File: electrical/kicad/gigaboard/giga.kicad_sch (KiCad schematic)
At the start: 61 parts, among them J1 Conn_01x04, J10 Conn_01x04, J11 Conn_01x06, J2 Conn_02x03_Top_Bottom, J3 Conn_01x04, J4 Conn_02x03_Top_Bottom, J5 Conn_02x03_Top_Bottom, J6 Conn_01x04, J7 Conn_02x03_Top_Bottom, J8 Conn_01x04, J9 Conn_02x03_Top_Bottom, U1 AHT20, U2 AS5600, U3 AS5600, U4 AS5600, U5 AS5600, U6 AS5600

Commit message: add(kicad): pbd files
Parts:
- removed A1: Arduino_Giga_R1_WiFi_Shield, PCM_arduino-library:Arduino_Giga_R1_WiFi_Shield, symbol PCM_arduino-library:Arduino_Giga_R1_WiFi_Shield_1
- removed C1, C2, C3, C4, C5, C6, C7, C8, C9: 100uF, Capacitor_THT:C_Radial_D4.0mm_H5.0mm_P1.50mm, symbol ControlPCB-rescue:CP1_Small
- removed D1, D2, D3, D4, D5: ~, TMC2209_SILENTSTEPSTICK:MODULE_TMC2209_SILENTSTEPSTICK, symbol Motor_Driver:TMC2209
- removed D6: MD10C_DC_Driver, symbol Motor_Driver:MD10C_DC_Driver
- removed J1, J10, J3, J6, J8: Conn_01x04, symbol Connector_Generic:Conn_01x04
- removed J11: Conn_01x06, symbol Connector_Generic:Conn_01x06
- removed J2, J4, J5, J7, J9: Conn_02x03_Top_Bottom, symbol Connector_Generic:Conn_02x03_Top_Bottom
- removed R1, R13, R2, R6, R9: 10k, symbol Device:R
- removed R10, R14, R16, R17, R3, R5, R7: 100k, symbol Device:R
- removed R11, R12, R15, R4, R8: 1K, symbol Device:R
- removed R18, R19, R20, R21, R22, R23, R24, R25, R26, R27: 3.9K, symbol Device:R
- removed S1: BMX160_9axis, symbol Sensors:BMX160_9axis
- removed U1: AHT20, AHT20:PSON100P300X300X110-6N, symbol AHT20:AHT20
- removed U2, U3, U4, U5, U6: AS5600, AS5600:AS5600, symbol AS5600:AS5600
- added A?: Arduino_Giga_R1_WiFi_Shield, PCM_arduino-library:Arduino_Giga_R1_WiFi_Shield, symbol PCM_arduino-library:Arduino_Giga_R1_WiFi_Shield_1
- added C? (x9): 100uF, Capacitor_THT:C_Radial_D4.0mm_H5.0mm_P1.50mm, symbol ControlPCB-rescue:CP1_Small
- added D? (x5): ~, TMC2209_SILENTSTEPSTICK:MODULE_TMC2209_SILENTSTEPSTICK, symbol Motor_Driver:TMC2209
- added D?: MD10C_DC_Driver, symbol Motor_Driver:MD10C_DC_Driver
- added J? (x5): Conn_01x04, symbol Connector_Generic:Conn_01x04
- added J? (x5): Conn_02x03_Top_Bottom, symbol Connector_Generic:Conn_02x03_Top_Bottom
- added J?: Conn_01x06, symbol Connector_Generic:Conn_01x06
- added R? (x5): 10k, symbol Device:R
- added R? (x5): 1K, symbol Device:R
- added R? (x7): 100k, symbol Device:R
- added R? (x10): 3.9K, symbol Device:R
- added S?: BMX160_9axis, symbol Sensors:BMX160_9axis
- added U? (x5): AS5600, AS5600:AS5600, symbol AS5600:AS5600
- added U?: AHT20, AHT20:PSON100P300X300X110-6N, symbol AHT20:AHT20
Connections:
- net +12V: now also C?.1, C?.1, C?.1, C?.1, C?.1, D?.8 (VM), D?.8 (VM), D?.8 (VM), D?.8 (VM), D?.8 (VM)
- net +3.3V: now also C?.1, J?.2 (Pin_2), U?.2 (VDD3V3), U?.2 (VDD3V3), U?.2 (VDD3V3), U?.2 (VDD3V3), U?.2 (VDD3V3)
- net +5V: now also A?.5V1 (5V), A?.5V2 (SPI_5V), A?.5V3 (5V), A?.5V4 (5V), A?.5V5 (5V), C?.1, D?.2 (VIO), D?.2 (VIO), D?.2 (VIO), D?.2 (VIO), D?.2 (VIO), J?.1 (Pin_1), J?.1 (Pin_1), J?.1 (Pin_1), J?.1 (Pin_1), J?.1 (Pin_1), J?.1 (Pin_1), J?.2 (Pin_2), J?.2 (Pin_2), J?.2 (Pin_2), J?.2 (Pin_2), J?.2 (Pin_2), J?.3 (Pin_3), J?.3 (Pin_3), J?.3 (Pin_3), J?.3 (Pin_3), J?.3 (Pin_3), R?.1, R?.1, R?.1, R?.1, R?.1, R?.1, R?.1, R?.1, R?.1, R?.1, R?.1, R?.1, R?.1, R?.1, R?.1, U?.1 (VDD5V), U?.1 (VDD5V), U?.1 (VDD5V), U?.1 (VDD5V), U?.1 (VDD5V)
- net D22: now also D?.18 (DIAG)
- net D23: now also D?.17 (INDEX)
- net D24: now also D?.18 (DIAG)
- net D25: now also D?.17 (INDEX)
- net D26: now also D?.18 (DIAG)
- net D27: now also D?.17 (INDEX)
- net D28: now also D?.18 (DIAG)
- net D29: now also D?.17 (INDEX)
- net D30: now also D?.18 (DIAG)
- net D31: now also D?.17 (INDEX)
- net DIR1: now also A?.D54, D?.9 (DIR), D?.9 (DIR), D?.9 (DIR), D?.9 (DIR), D?.9 (DIR)
- net DIR2: now also A?.D57
- net DIR3: now also A?.D60
- net DIR4: now also A?.D63
- net DIR5: now also A?.D66
- net ENA1: now also A?.D56, D?.16 (~{EN}), D?.16 (~{EN}), D?.16 (~{EN}), D?.16 (~{EN}), D?.16 (~{EN}), R?.2, R?.2, R?.2, R?.2, R?.2
- net ENA2: now also A?.D59
- net ENA3: now also A?.D62
- net ENA4: now also A?.D65
- net ENA5: now also A?.D68
- net GND: now also A?.GND1 (GND), A?.GND10 (GND), A?.GND11 (GND), A?.GND12 (GND), A?.GND13 (GND), A?.GND14 (GND), A?.GND15 (GND), A?.GND2 (GND), A?.GND3 (GND), A?.GND4 (SPI_GND), A?.GND5 (GND), A?.GND6 (GND), A?.GND7 (GND), A?.GND8 (GND), A?.GND9 (GND), C?.2, C?.2, C?.2, C?.2, C?.2, C?.2, C?.2, C?.2, C?.2, D?.1 (GND), D?.1 (GND), D?.1 (GND), D?.1 (GND), D?.1 (GND), D?.2 (GND), D?.7 (GND), D?.7 (GND), D?.7 (GND), D?.7 (GND), D?.7 (GND), J?.3 (Pin_3), R?.2, R?.2, R?.2, R?.2, R?.2, S?.2 (GND), U?.4 (GND), U?.4 (GND), U?.4 (GND), U?.4 (GND), U?.4 (GND), U?.5 (GND), U?.8 (DIR), U?.8 (DIR), U?.8 (DIR), U?.8 (DIR), U?.8 (DIR)
- net OUT: now also J?.6 (Pin_6), U?.3 (OUT), U?.3 (OUT), U?.3 (OUT), U?.3 (OUT), U?.3 (OUT)
- net PUL1: now also A?.D55, D?.10 (STEP), D?.10 (STEP), D?.10 (STEP), D?.10 (STEP), D?.10 (STEP)
- net PUL2: now also A?.D58
- net PUL3: now also A?.D61
- net PUL4: now also A?.D64
- net PUL5: now also A?.D67
- net SCL1: now also J?.4 (Pin_4), R?.2, R?.2, R?.2, R?.2, R?.2, U?.7 (SCL), U?.7 (SCL), U?.7 (SCL), U?.7 (SCL), U?.7 (SCL)
- net SCL2: now also R?.1, S?.3 (SCL), U?.3 (SCL)
- net SDA1: now also J?.5 (Pin_5), R?.2, R?.2, R?.2, R?.2, R?.2, U?.6 (SDA), U?.6 (SDA), U?.6 (SDA), U?.6 (SDA), U?.6 (SDA)
- net SDA2: now also R?.1, S?.4 (SDA), U?.4 (SDA)
- net URT1: now also A?.D0 (D0/RX0), A?.D1 (D1/TX0), D?.12 (UART), D?.12 (UART), D?.12 (UART), D?.12 (UART), D?.12 (UART), R?.2, R?.2, R?.2, R?.2, R?.2
- net URT2: now also A?.D18 (D18/TX1), A?.D19 (D19/RX1)
- net URT3: now also A?.D16 (D16/TX2), A?.D17 (D17/RX2)
- net URT4: now also A?.D14 (D14/TX3), A?.D15 (D15/RX3)
- net URT5: now also A?.D20 (D20/SDA), A?.D21 (D21/SCL)
- net cs: now also S?.7 (CSB)
- new net: D?.6 (2B), J?.1 (Pin_1) (x5)
- new net: D?.5 (2A), J?.2 (Pin_2) (x5)
- new net: D?.4 (1A), J?.3 (Pin_3) (x5)
- new net: D?.3 (1B), J?.4 (Pin_4) (x5)
- new net: D?.11 (PDN), R?.1 (x5)
- new net: D?.15 (MS1), J?.4 (Pin_4), R?.1 (x5)
- new net: D?.14 (MS2), J?.5 (Pin_5) (x5)
- new net: D?.13 (SPRD), J?.6 (Pin_6) (x5)
- new net: C?.1, S?.1 (VCC)
- new net: C?.1, R?.2, R?.2, U?.2 (VDD)
- new net: U?.1 (NC), U?.6 (NC)

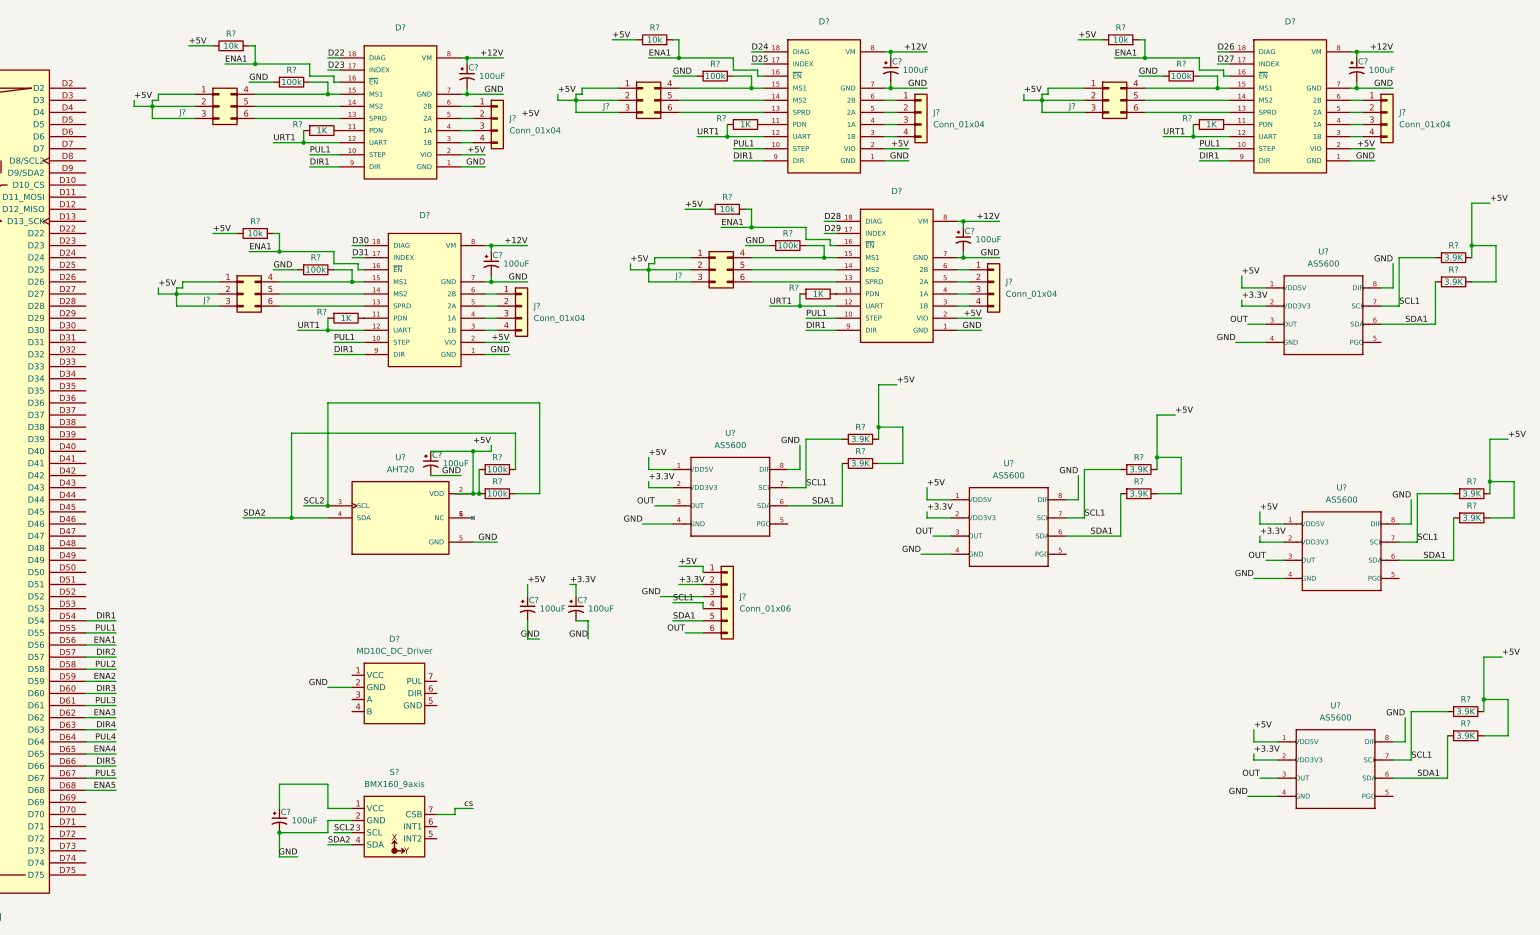
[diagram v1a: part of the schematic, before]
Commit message: update(giga): change symbols
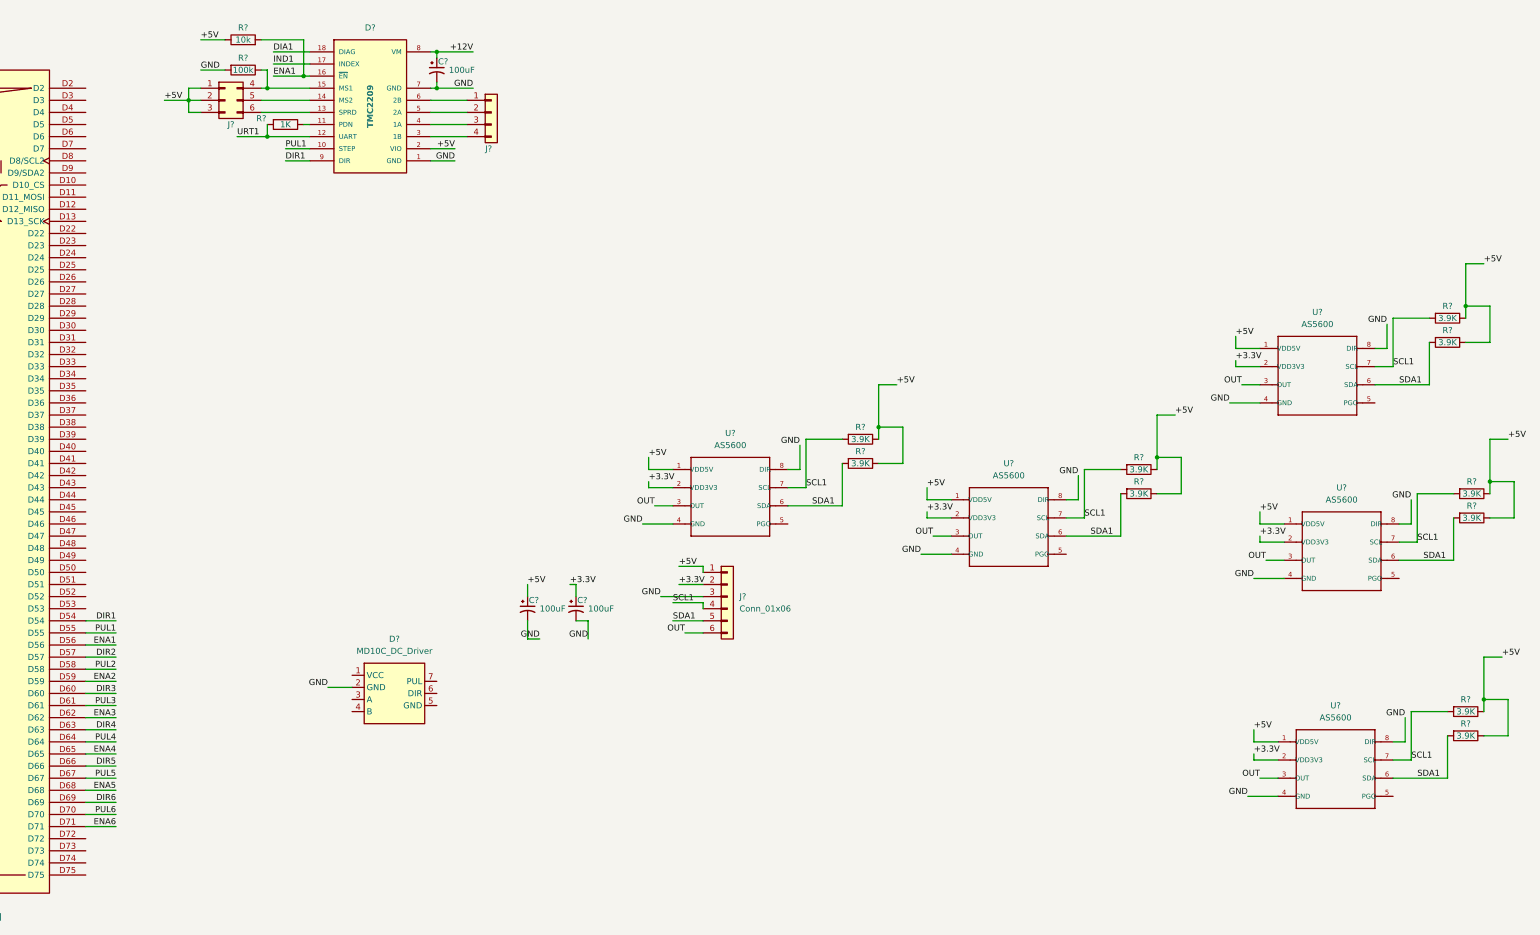
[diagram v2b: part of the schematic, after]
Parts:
- removed C? (x6): 100uF, Capacitor_THT:C_Radial_D4.0mm_H5.0mm_P1.50mm, symbol ControlPCB-rescue:CP1_Small
- removed D? (x5): ~, TMC2209_SILENTSTEPSTICK:MODULE_TMC2209_SILENTSTEPSTICK, symbol Motor_Driver:TMC2209
- removed J? (x4): Conn_01x04, symbol Connector_Generic:Conn_01x04
- removed J? (x4): Conn_02x03_Top_Bottom, symbol Connector_Generic:Conn_02x03_Top_Bottom
- removed R? (x4): 10k, symbol Device:R
- removed R? (x4): 1K, symbol Device:R
- removed R? (x6): 100k, symbol Device:R
- removed S?: BMX160_9axis, symbol Sensors:BMX160_9axis
- removed U?: AHT20, AHT20:PSON100P300X300X110-6N, symbol AHT20:AHT20
- added D?: TMC2209, TMC2209_SILENTSTEPSTICK:MODULE_TMC2209_SILENTSTEPSTICK, symbol Motor_Driver:TMC2209
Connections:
- net +12V: now also D?.8 (VM)
- net +5V: now also D?.2 (VIO)
- net DIR1: now also D?.9 (DIR)
- net ENA1: now also D?.16 (~{EN})
- net GND: now also D?.1 (GND), D?.7 (GND)
- net PUL1: now also D?.10 (STEP)
- net URT1: now also D?.12 (UART)
- net DIR6: now reaches A?.D69
- net PUL6: now reaches A?.D70
- net ENA6: now reaches A?.D71
- net at J?.4 (Pin_4), R?.1: now also D?.15 (MS1)
- net at J?.1 (Pin_1): now also D?.6 (2B)
- net at J?.2 (Pin_2): now also D?.5 (2A)
- net at J?.3 (Pin_3): now also D?.4 (1A)
- net at J?.4 (Pin_4): now also D?.3 (1B)
- net at J?.5 (Pin_5): now also D?.14 (MS2)
- net at J?.6 (Pin_6): now also D?.13 (SPRD)
- net at R?.1: now also D?.11 (PDN)
- new net DIA1: D?.18 (DIAG)
- new net IND1: D?.17 (INDEX)
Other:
- moved on the sheet: C?, J?, R?, U?

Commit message: update(giga): sym structure, comms module
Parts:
- removed C? (x3): 100uF, Capacitor_THT:C_Radial_D4.0mm_H5.0mm_P1.50mm, symbol ControlPCB-rescue:CP1_Small
- removed D?: MD10C_DC_Driver, symbol Motor_Driver:MD10C_DC_Driver
- removed D?: TMC2209, TMC2209_SILENTSTEPSTICK:MODULE_TMC2209_SILENTSTEPSTICK, symbol Motor_Driver:TMC2209
- removed J?: Conn_01x06, symbol Connector_Generic:Conn_01x06
- removed J?: Conn_01x04, symbol Connector_Generic:Conn_01x04
- removed J?: Conn_02x03_Top_Bottom, symbol Connector_Generic:Conn_02x03_Top_Bottom
- removed R?: 100k, symbol Device:R
- removed R? (x10): 3.9K, symbol Device:R
- removed R?: 10k, symbol Device:R
- removed R?: 1K, symbol Device:R
- removed U? (x5): AS5600, AS5600:AS5600, symbol AS5600:AS5600
- added C? (x6): 100uF, Capacitor_THT:C_Radial_D4.0mm_H5.0mm_P1.50mm, symbol ControlPCB-rescue:CP1_Small
- added D? (x6): TMC2209, TMC2209_SILENTSTEPSTICK:MODULE_TMC2209_SILENTSTEPSTICK, symbol Motor_Driver:TMC2209
- added E? (x6): AS5600, symbol Sensors:AS5600_Encoder
- added J? (x13): Conn_01x04, symbol Connector_Generic:Conn_01x04
- added J? (x2): Conn_01x02, symbol Connector_Generic:Conn_01x02
- added J? (x6): Conn_02x04_Counter_Clockwise, symbol Connector_Generic:Conn_02x04_Counter_Clockwise
- added J?: Screw_Terminal_01x03, symbol Connector:Screw_Terminal_01x03
- added R? (x6): 10k, symbol Device:R
- added R? (x6): 100k, symbol Device:R
- added S?: INA219, symbol Sensors:INA219_Current_Voltage_Sensor
- added U?: TCA9548A, 2717:MODULE_2717, symbol Comms:TCA9548A
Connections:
- net +3.3V: now also A?.3V1 (3.3V)
- net +5V: now also D?.2 (VIO), D?.2 (VIO), D?.2 (VIO), D?.2 (VIO), D?.2 (VIO), D?.2 (VIO), E?.1 (VCC), E?.1 (VCC), E?.1 (VCC), E?.1 (VCC), E?.1 (VCC), E?.1 (VCC), J?.1 (Pin_1), J?.1 (Pin_1), J?.1 (Pin_1), J?.1 (Pin_1), J?.1 (Pin_1), J?.1 (Pin_1), J?.2 (Pin_2), J?.2 (Pin_2), J?.2 (Pin_2), J?.2 (Pin_2), J?.2 (Pin_2), J?.2 (Pin_2), J?.3 (Pin_3), J?.3 (Pin_3), J?.3 (Pin_3), J?.3 (Pin_3), J?.3 (Pin_3), J?.3 (Pin_3), J?.3 (Pin_3), R?.1, R?.1, R?.1, R?.1, R?.1, R?.1, S?.4 (VCC)
- net GND: now also C?.2, C?.2, C?.2, C?.2, C?.2, C?.2, D?.1 (GND), D?.1 (GND), D?.1 (GND), D?.1 (GND), D?.1 (GND), D?.1 (GND), D?.7 (GND), D?.7 (GND), D?.7 (GND), D?.7 (GND), D?.7 (GND), D?.7 (GND), E?.3 (GND), E?.3 (GND), E?.3 (GND), E?.3 (GND), E?.3 (GND), E?.3 (GND), E?.7 (GPO), E?.7 (GPO), E?.7 (GPO), E?.7 (GPO), E?.7 (GPO), E?.7 (GPO), J?.2 (Pin_2), R?.2, R?.2, R?.2, R?.2, R?.2, R?.2, S?.2 (VIN-), S?.3 (GND)
- net DIR1: no longer names the net of A?.D54
- net DIR2: no longer names the net of A?.D57
- net DIR3: no longer names the net of A?.D60
- net DIR4: no longer names the net of A?.D63
- net DIR5: no longer names the net of A?.D66
- net DIR6: no longer names the net of A?.D69
- net ENA1: no longer names the net of A?.D56
- net ENA2: no longer names the net of A?.D59
- net ENA3: no longer names the net of A?.D62
- net ENA4: no longer names the net of A?.D65
- net ENA5: no longer names the net of A?.D68
- net ENA6: no longer names the net of A?.D71
- net PUL1: no longer names the net of A?.D55
- net PUL2: no longer names the net of A?.D58
- net PUL3: no longer names the net of A?.D61
- net PUL4: no longer names the net of A?.D64
- net PUL5: no longer names the net of A?.D67
- net PUL6: no longer names the net of A?.D70
- net URT1: no longer names the net of A?.D0 (D0/RX0)
- net URT1: no longer A?.D1 (D1/TX0)
- net URT2: no longer names the net of A?.D18 (D18/TX1)
- net URT2: no longer A?.D19 (D19/RX1)
- net URT3: no longer names the net of A?.D16 (D16/TX2)
- net URT3: no longer A?.D17 (D17/RX2)
- net URT4: no longer names the net of A?.D14 (D14/TX3)
- net URT4: no longer A?.D15 (D15/RX3)
- net URT5: no longer names the net of A?.D20 (D20/SDA)
- net URT5: no longer A?.D21 (D21/SCL)
- new net: D?.11 (PDN), D?.12 (UART), J?.5 (Pin_5) (x6)
- new net: D?.13 (SPRD), J?.6 (Pin_6) (x6)
- new net: D?.14 (MS2), J?.7 (Pin_7) (x6)
- new net: D?.15 (MS1), J?.8 (Pin_8), R?.1 (x6)
- new net: D?.3 (1B), J?.4 (Pin_4) (x6)
- new net: D?.4 (1A), J?.3 (Pin_3) (x6)
- new net: D?.5 (2A), J?.2 (Pin_2) (x6)
- new net: D?.6 (2B), J?.1 (Pin_1) (x6)
- new net +4S: J?.1 (Pin_1), S?.1 (VIN+)
- new net AS1_DIR: E?.4 (DIR)
- new net AS1_OUT: E?.2 (OUT)
- new net AS1_SCL: E?.6 (SDA)
- new net AS1_SDA: E?.5 (SCL)
- new net AS2_DIR: E?.4 (DIR)
- new net AS2_OUT: E?.2 (OUT)
- new net AS2_SCL: E?.6 (SDA)
- new net AS2_SDA: E?.5 (SCL)
- new net AS3_DIR: E?.4 (DIR)
- new net AS3_OUT: E?.2 (OUT)
- new net AS3_SCL: E?.6 (SDA)
- new net AS3_SDA: E?.5 (SCL)
- new net AS4_DIR: E?.4 (DIR)
- new net AS4_OUT: E?.2 (OUT)
- new net AS4_SCL: E?.6 (SDA)
- new net AS4_SDA: E?.5 (SCL)
- new net AS5_DIR: E?.4 (DIR)
- new net AS5_OUT: E?.2 (OUT)
- new net AS5_SCL: E?.6 (SDA)
- new net AS5_SDA: E?.5 (SCL)
- new net AS6_DIR: E?.4 (DIR)
- new net AS6_OUT: E?.2 (OUT)
- new net AS6_SCL: E?.6 (SDA)
- new net AS6_SDA: E?.5 (SCL)
- new net DC1_CHA: J?.3 (Pin_3)
- new net DC1_CHB: J?.4 (Pin_4)
- new net DC1_DIR: J?.2 (Pin_2)
- new net DC1_PWM: J?.1 (Pin_1)
- new net DC2_CHA: J?.3 (Pin_3)
- new net DC2_CHB: J?.4 (Pin_4)
- new net DC2_DIR: J?.2 (Pin_2)
- new net DC2_PWM: J?.1 (Pin_1)
- new net DC3_CHA: J?.3 (Pin_3)
- new net DC3_CHB: J?.4 (Pin_4)
- new net DC3_DIR: J?.2 (Pin_2)
- new net DC3_PWM: J?.1 (Pin_1)
- new net DC4_CHA: J?.3 (Pin_3)
- new net DC4_CHB: J?.4 (Pin_4)
- new net DC4_DIR: J?.2 (Pin_2)
- new net DC4_PWM: J?.1 (Pin_1)
- new net DC5_CHA: J?.3 (Pin_3)
- new net DC5_CHB: J?.4 (Pin_4)
- new net DC5_DIR: J?.2 (Pin_2)
- new net DC5_PWM: J?.1 (Pin_1)
- new net DC6_CHA: J?.3 (Pin_3)
- new net DC6_CHB: J?.4 (Pin_4)
- new net DC6_DIR: J?.2 (Pin_2)
- new net DC6_PWM: J?.1 (Pin_1)
- new net INA_SCL: S?.6 (SDA)
- new net INA_SDA: S?.5 (SCL)
- new net NAN0_TX: J?.2 (Pin_2)
- new net NANO_RX: J?.1 (Pin_1)
- new net Pi5_RX: J?.1 (Pin_1)
- new net Pi5_TX: J?.2 (Pin_2)
- new net ST1_DIA: D?.18 (DIAG)
- new net ST1_DIR: D?.9 (DIR)
- new net ST1_ENA: D?.16 (~{EN}), R?.2
- new net ST1_IND: D?.17 (INDEX)
- new net ST1_STP: D?.10 (STEP)
- new net ST1_URT: J?.4 (Pin_4)
- new net ST2_DIA: D?.18 (DIAG)
- new net ST2_DIR: D?.9 (DIR)
- new net ST2_ENA: D?.16 (~{EN}), R?.2
- new net ST2_IND: D?.17 (INDEX)
- new net ST2_STP: D?.10 (STEP)
- new net ST2_URT: J?.4 (Pin_4)
- new net ST3_DIA: D?.18 (DIAG)
- new net ST3_DIR: D?.9 (DIR)
- new net ST3_ENA: D?.16 (~{EN}), R?.2
- new net ST3_IND: D?.17 (INDEX)
- new net ST3_STP: D?.10 (STEP)
- new net ST3_URT: J?.4 (Pin_4)
- new net ST4_DIA: D?.18 (DIAG)
- new net ST4_DIR: D?.9 (DIR)
- new net ST4_ENA: D?.16 (~{EN}), R?.2
- new net ST4_IND: D?.17 (INDEX)
- new net ST4_STP: D?.10 (STEP)
- new net ST4_URT: J?.4 (Pin_4)
- new net ST5_DIA: D?.18 (DIAG)
- new net ST5_DIR: D?.9 (DIR)
- new net ST5_ENA: D?.16 (~{EN}), R?.2
- new net ST5_IND: D?.17 (INDEX)
- new net ST5_STP: D?.10 (STEP)
- new net ST5_URT: J?.4 (Pin_4)
- new net ST6_DIA: D?.18 (DIAG)
- new net ST6_DIR: D?.9 (DIR)
- new net ST6_ENA: D?.16 (~{EN}), R?.2
- new net ST6_IND: D?.17 (INDEX)
- new net ST6_STP: D?.10 (STEP)
- new net ST6_URT: J?.4 (Pin_4)
- new net SV1_PWM: J?.1 (Pin_1)
- new net SV2_PWM: J?.2 (Pin_2)
- new net SV3_PWM: J?.3 (Pin_3)
- new net SV4_PWM: J?.4 (Pin_4)
- new net VM: C?.1, C?.1, C?.1, C?.1, C?.1, C?.1, D?.8 (VM), D?.8 (VM), D?.8 (VM), D?.8 (VM), D?.8 (VM), D?.8 (VM)
- no-connect marks 0 -> 2
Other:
- moved on the sheet: A?

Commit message: add(elec): images in readme
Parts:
- removed A?: Arduino_Giga_R1_WiFi_Shield, PCM_arduino-library:Arduino_Giga_R1_WiFi_Shield, symbol PCM_arduino-library:Arduino_Giga_R1_WiFi_Shield_1
- added A?: Arduino GIGA R1 WiFi, MCU:Arduino_Giga_R1, symbol MCU:Arduino_Giga-R1
- added C?: C, symbol Device:C
- added F?: Fuse, symbol Device:Fuse
- added Q?: PMOS, symbol Simulation_SPICE:PMOS
- added Q?: BS108, Package_TO_SOT_THT:TO-92_Inline, symbol Transistor_FET:BS108
- added R?: R, symbol Device:R
- added SW?: SW_DIP_x01, symbol Switch:SW_DIP_x01
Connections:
- net AS1_DIR is gone; now on net GND: E?.4 (DIR)
- net AS2_DIR is gone; now on net GND: E?.4 (DIR)
- net AS3_DIR is gone; now on net GND: E?.4 (DIR)
- net AS4_DIR is gone; now on net GND: E?.4 (DIR)
- net AS5_DIR is gone; now on net GND: E?.4 (DIR)
- net AS6_DIR is gone; now on net GND: E?.4 (DIR)
- net NAN0_TX is gone; now on net NANO_RX: J?.2 (Pin_2)
- net +3.3V: now also A?.3V3 (3.3V)
- net +4S: now also F?.1
- net +5V: now also U?.1 (VIN), A?.5V, A?.VIN; no longer J?.1 (Pin_1), J?.2 (Pin_2), J?.3 (Pin_3)
- net AS1_SCL: now also U?.13 (SDA2)
- net AS1_SDA: now also U?.14 (SCL2)
- net AS2_SCL: now also U?.15 (SDA3)
- net AS2_SDA: now also U?.16 (SCL3)
- net AS3_SCL: now also U?.17 (SDA4)
- net AS3_SDA: now also U?.18 (SCL4)
- net AS4_SCL: now also U?.19 (SDA5)
- net AS4_SDA: now also U?.20 (SCL5)
- net AS5_SCL: now also U?.21 (SDA6)
- net AS5_SDA: now also U?.22 (SCL6)
- net AS6_SCL: now also U?.23 (SDA7)
- net AS6_SDA: now also U?.24 (SCL7)
- net DC1_CHA: now also A?.D31
- net DC1_CHB: now also A?.D32
- net DC1_DIR: now also A?.D30
- net DC1_PWM: now also A?.D2
- net DC2_CHA: now also A?.D34
- net DC2_CHB: now also A?.D35
- net DC2_DIR: now also A?.D33
- net DC2_PWM: now also A?.D3
- net DC3_CHA: now also A?.D37
- net DC3_CHB: now also A?.D38
- net DC3_DIR: now also A?.D36
- net DC3_PWM: now also A?.D4
- net DC4_CHA: now also A?.D40
- net DC4_CHB: now also A?.D41
- net DC4_DIR: now also A?.D39
- net DC4_PWM: now also A?.D5
- net DC5_CHA: now also A?.D43
- net DC5_CHB: now also A?.D44
- net DC5_DIR: now also A?.D42
- net DC5_PWM: now also A?.D6
- net DC6_CHA: now also A?.D46
- net DC6_CHB: now also A?.D47
- net DC6_DIR: now also A?.D45
- net DC6_PWM: now also A?.D7
- net GND: now also U?.2 (GND), U?.6 (A0), U?.7 (A1), U?.8 (A2), A?.GND
- net INA_SCL: now also A?.SDA1 (D102/SDA1)
- net INA_SDA: now also A?.SCL1 (D101/SCL1)
- net NANO_RX: now also A?.D18 (D18/TX1); no longer J?.1 (Pin_1)
- net Pi5_RX: now also J?.2 (Pin_2), A?.D1 (D1/TX0); no longer J?.1 (Pin_1)
- net Pi5_TX: now also J?.1 (Pin_1), A?.D0 (D0/RX0); no longer J?.2 (Pin_2)
- net ST1_DIR: now also A?.D53
- net ST1_ENA: now also A?.D51
- net ST1_STP: now also A?.D52
- net ST2_DIR: now also A?.D56
- net ST2_ENA: now also A?.D54
- net ST2_STP: now also A?.D55
- net ST3_DIR: now also A?.D59
- net ST3_ENA: now also A?.D57
- net ST3_STP: now also A?.D58
- net ST4_DIR: now also A?.D62
- net ST4_ENA: now also A?.D60
- net ST4_STP: now also A?.D61
- net ST5_DIR: now also A?.D65
- net ST5_ENA: now also A?.D63
- net ST5_STP: now also A?.D64
- net ST6_DIR: now also A?.D68
- net ST6_ENA: now also A?.D66
- net ST6_STP: now also A?.D67
- net SV1_PWM: now also A?.D10 (D10_CS)
- net SV2_PWM: now also A?.D11 (D11_MOSI)
- net SV3_PWM: now also A?.D12 (D12_MISO)
- net SV4_PWM: now also A?.D13 (D13_SCK)
- net TCA_SCL: now reaches U?.3 (SDA)
- net TCA_SCL: now also A?.D20 (D20/SDA)
- net TCA_SDA: now reaches U?.4 (SCL)
- net TCA_SDA: now also A?.D21 (D21/SCL)
- net TCA_RST: now reaches U?.5 (RST)
- net TCA_RST: now also A?.D22
- net ST1_DIA: no longer names the net of D?.18 (DIAG)
- net ST1_IND: no longer names the net of D?.17 (INDEX)
- net ST4_DIA: no longer names the net of D?.18 (DIAG)
- net ST4_IND: no longer names the net of D?.17 (INDEX)
- new net E-STOP: A?.D23
- new net NANO_TX: A?.D19 (D19/RX1), J?.1 (Pin_1)
- new net STP_MS1: A?.D48, J?.1 (Pin_1)
- new net STP_MS2: A?.D49, J?.2 (Pin_2)
- new net STP_MS3: A?.D50, J?.3 (Pin_3)
- no-connect marks 2 -> 25
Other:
- moved on the sheet: C?, D?, E?, J?, R?, S?, U?
